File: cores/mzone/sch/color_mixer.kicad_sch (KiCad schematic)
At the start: 17 parts

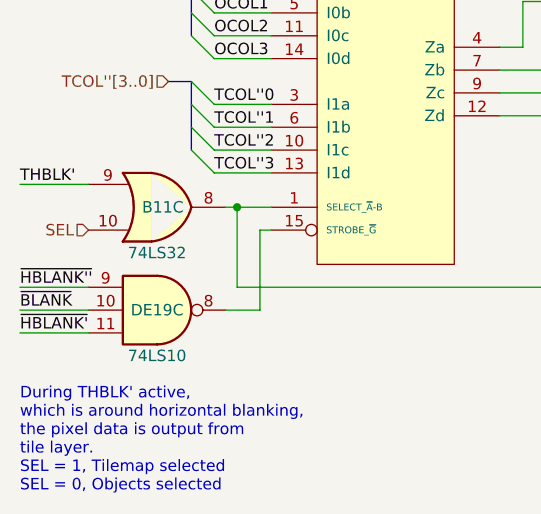
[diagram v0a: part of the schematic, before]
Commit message: mzone sim working, no sound.
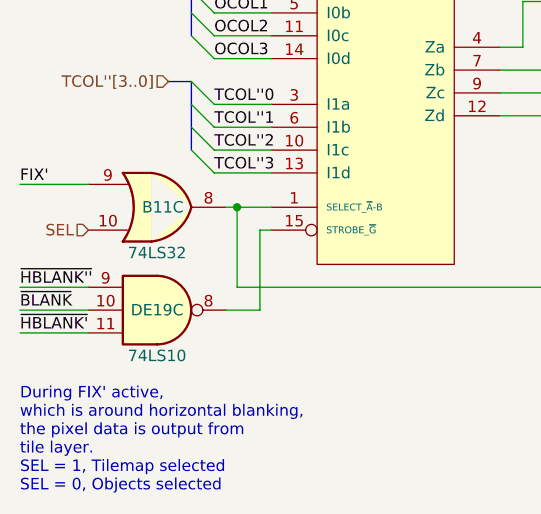
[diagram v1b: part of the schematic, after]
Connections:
- net THBLK' renamed FIX'
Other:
- note added: "During FIX' active, which is around horizontal blanking, the pixel data is output from tile layer. SEL = 1, Tilemap selected SEL = 0, Objects selected"
- note removed: "During THBLK' active, which is around horizontal blanking, the pixel data is output from tile layer. SEL = 1, Tilemap selected SEL = 0, Objects selected"
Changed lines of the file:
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@@
 		)
 	)
-	(text "During THBLK' active,\nwhich is around horizontal blanking,\nthe pixel data is output from\ntile layer.\nSEL = 1, Tilemap selected\nSEL = 0, Objects selected"
+	(text "During FIX' active,\nwhich is around horizontal blanking,\nthe pixel data is output from\ntile layer.\nSEL = 1, Tilemap selected\nSEL = 0, Objects selected"
 		(exclude_from_sim no)
 		(at 138.43 199.39 0)
@@
 		)
 	)
-	(label "THBLK'"
+	(label "FIX'"
 		(at 138.43 165.1 0)
 		(fields_autoplaced yes)

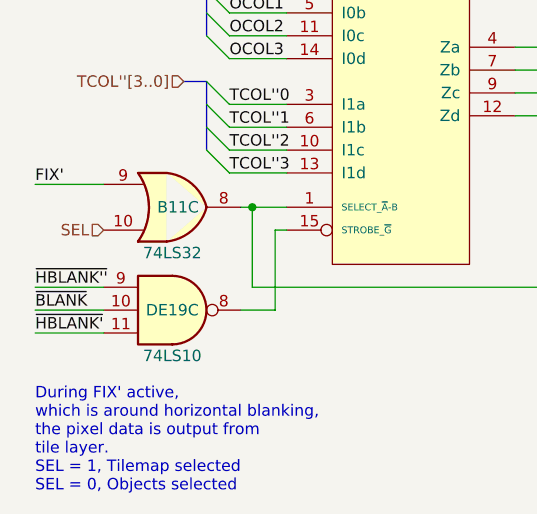
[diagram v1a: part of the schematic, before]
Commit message: mzone core
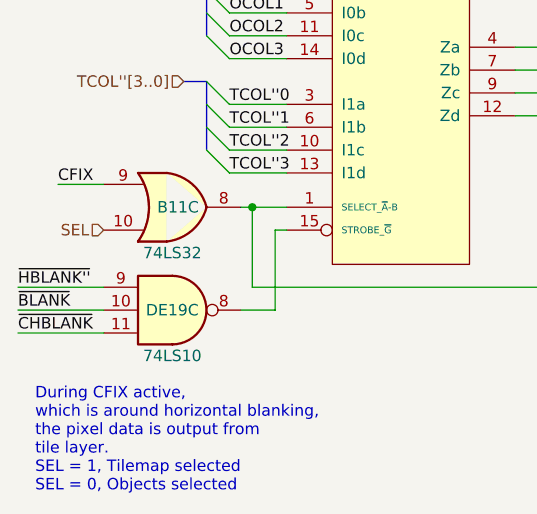
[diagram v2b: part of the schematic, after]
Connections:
- net FIX' renamed CFIX
- net ~{HBLANK'} renamed ~{CHBLANK}
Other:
- note added: "During CFIX active, which is around horizontal blanking, the pixel data is output from tile layer. SEL = 1, Tilemap selected SEL = 0, Objects selected"
- note removed: "During FIX' active, which is around horizontal blanking, the pixel data is output from tile layer. SEL = 1, Tilemap selected SEL = 0, Objects selected"
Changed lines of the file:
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@@
 	(wire
 		(pts
-			(xy 138.43 181.61) (xy 146.05 181.61)
+			(xy 136.525 181.61) (xy 146.05 181.61)
 		)
 		(stroke
@@
 	(wire
 		(pts
-			(xy 138.43 179.07) (xy 146.05 179.07)
+			(xy 136.525 179.07) (xy 146.05 179.07)
 		)
 		(stroke
@@
 	(wire
 		(pts
-			(xy 138.43 176.53) (xy 146.05 176.53)
+			(xy 136.525 176.53) (xy 146.05 176.53)
 		)
 		(stroke
@@
 	(wire
 		(pts
-			(xy 138.43 165.1) (xy 146.05 165.1)
+			(xy 140.97 165.1) (xy 146.05 165.1)
 		)
 		(stroke
@@
 		)
 	)
-	(text "During FIX' active,\nwhich is around horizontal blanking,\nthe pixel data is output from\ntile layer.\nSEL = 1, Tilemap selected\nSEL = 0, Objects selected"
+	(text "During CFIX active,\nwhich is around horizontal blanking,\nthe pixel data is output from\ntile layer.\nSEL = 1, Tilemap selected\nSEL = 0, Objects selected"
 		(exclude_from_sim no)
 		(at 138.43 199.39 0)
@@
 	)
 	(label "~{BLANK}"
-		(at 138.43 179.07 0)
+		(at 136.525 179.07 0)
 		(fields_autoplaced yes)
 		(effects
@@
 		)
 	)
-	(label "FIX'"
-		(at 138.43 165.1 0)
+	(label "CFIX"
+		(at 140.97 165.1 0)
 		(fields_autoplaced yes)
 		(effects
@@
 		)
 	)
-	(label "~{HBLANK'}"
-		(at 138.43 181.61 0)
+	(label "~{CHBLANK}"
+		(at 136.525 181.61 0)
 		(fields_autoplaced yes)
 		(effects
@@
 	)
 	(label "~{HBLANK''}"
-		(at 138.43 176.53 0)
-		(fields_autoplaced yes)
-		(effects
+		(at 136.525 176.53 0)
+		(fields_autoplaced yes)
+		(effects
